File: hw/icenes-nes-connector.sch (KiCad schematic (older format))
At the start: 5 parts

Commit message: .
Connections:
- net FPGA_CPU_D7: no longer U?.26 (2A8)
- net NES_CPU_D7: no longer U?.23 (2B8)
- net NES_PPU_D7: now also U?.23 (2B8)
- new net FPGA_PPU_D7: U?.26 (2A8)
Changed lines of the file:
@@
 FPGA_PPU_D6
 Text GLabel 1550 5800 0    50   BiDi ~ 0
-FPGA_CPU_D7
+FPGA_PPU_D7
 Text GLabel 1550 5950 0    50   Input ~ 0
 ~PPU_DATA_OE
@@
 	2850 5700 3450 5700
 Text Label 3450 5800 2    50   ~ 0
-NES_CPU_D7
+NES_PPU_D7
 Wire Wire Line
 	2850 5800 3450 5800

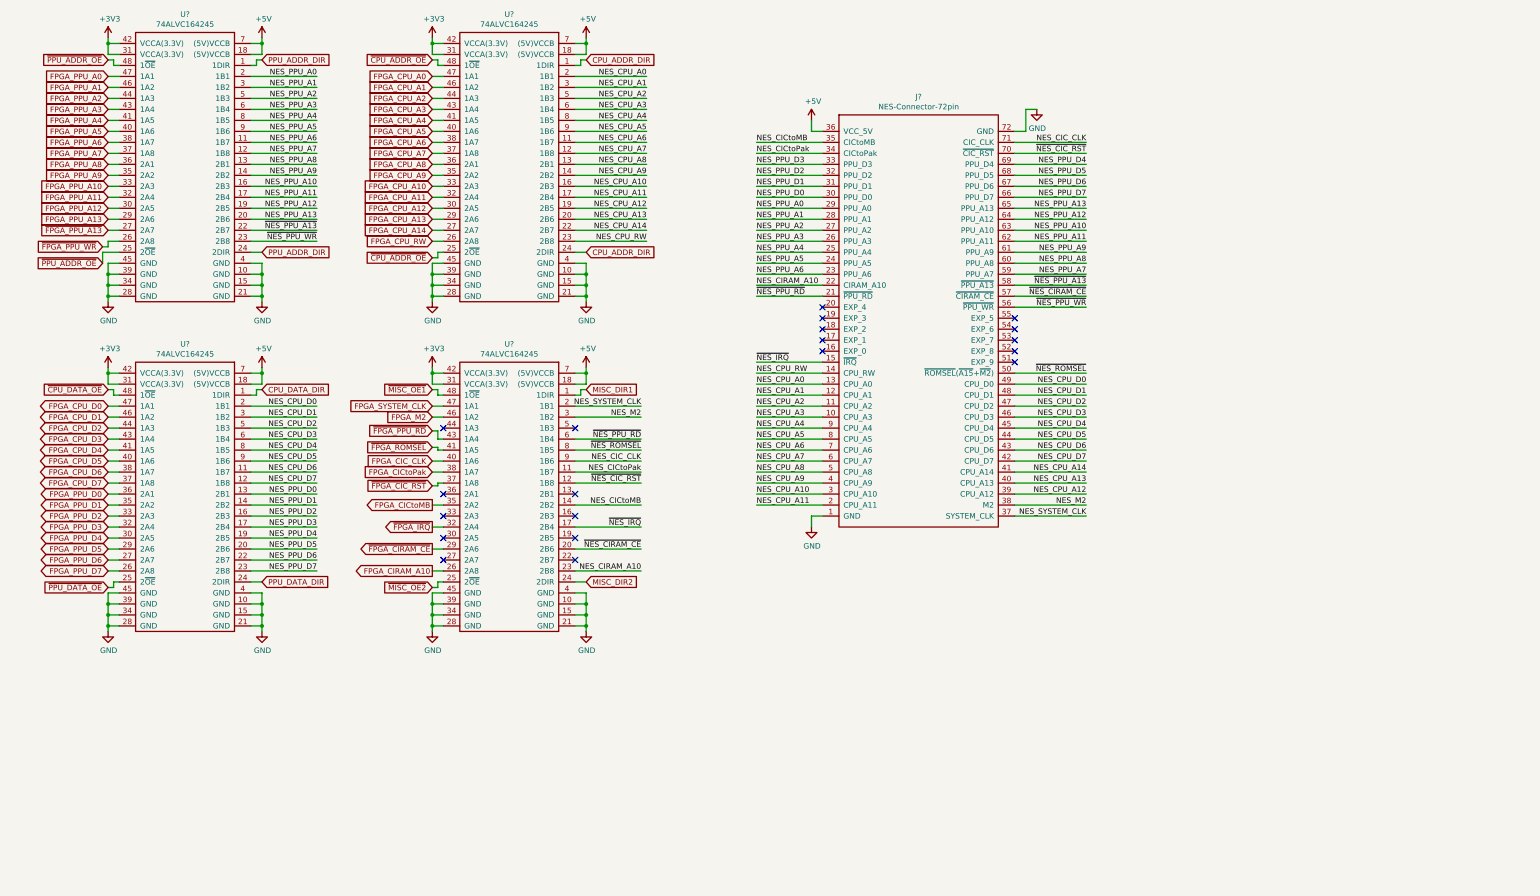
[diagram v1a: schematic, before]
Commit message: Added voltage generators for 3.3V, 1.2V and 5V. Added more info and footprints to some components. Connected signals to the NES connector to banks 0 and 1.
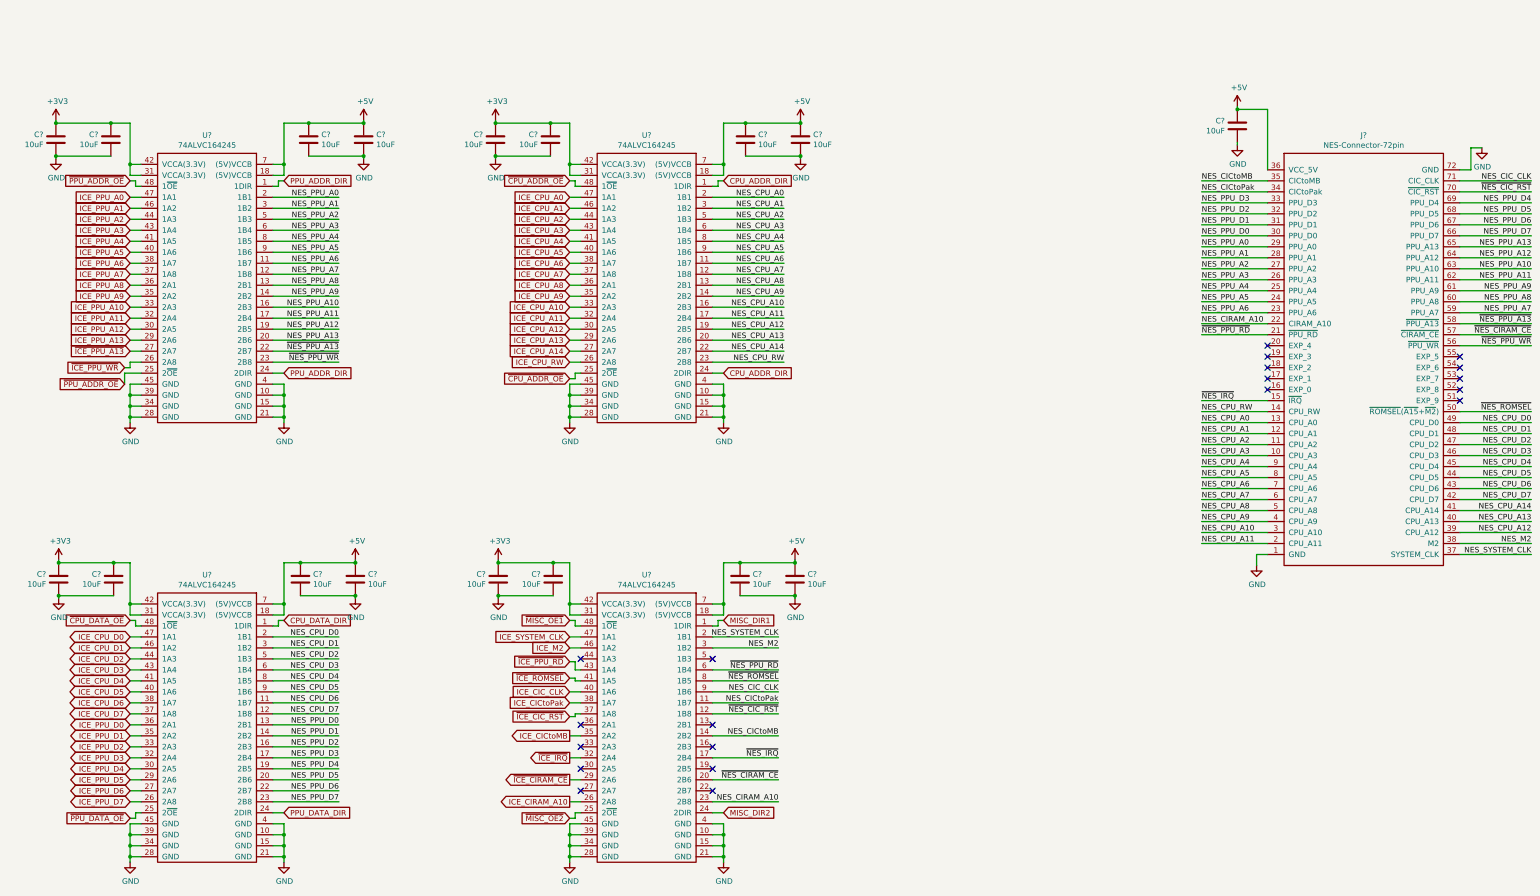
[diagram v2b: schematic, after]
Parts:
- added C? (x17): C10uF, Capacitor_SMD:C_0603_1608Metric_Pad1.05x0.95mm_HandSolder, symbol icenes-library:C10uF
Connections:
- net +3V3: now also C?.2, C?.2, C?.2, C?.2, C?.2, C?.2, C?.2, C?.2
- net +5V: now also C?.1, C?.1, C?.1, C?.1, C?.1, C?.1, C?.1, C?.1, C?.2
- net GND: now also C?.1, C?.1, C?.1, C?.1, C?.1, C?.1, C?.1, C?.1, C?.1, C?.2, C?.2, C?.2, C?.2, C?.2, C?.2, C?.2, C?.2
- net FPGA_CIC_CLK renamed ICE_CIC_CLK
- net FPGA_CICtoMB renamed ICE_CICtoMB
- net FPGA_CICtoPak renamed ICE_CICtoPak
- net FPGA_CIRAM_A10 renamed ICE_CIRAM_A10
- net FPGA_CPU_A0 renamed ICE_CPU_A0
- net FPGA_CPU_A1 renamed ICE_CPU_A1
- net FPGA_CPU_A10 renamed ICE_CPU_A10
- net FPGA_CPU_A11 renamed ICE_CPU_A11
- net FPGA_CPU_A12 renamed ICE_CPU_A12
- net FPGA_CPU_A13 renamed ICE_CPU_A13
- net FPGA_CPU_A14 renamed ICE_CPU_A14
- net FPGA_CPU_A2 renamed ICE_CPU_A2
- net FPGA_CPU_A3 renamed ICE_CPU_A3
- net FPGA_CPU_A4 renamed ICE_CPU_A4
- net FPGA_CPU_A5 renamed ICE_CPU_A5
- net FPGA_CPU_A6 renamed ICE_CPU_A6
- net FPGA_CPU_A7 renamed ICE_CPU_A7
- net FPGA_CPU_A8 renamed ICE_CPU_A8
- net FPGA_CPU_A9 renamed ICE_CPU_A9
- net FPGA_CPU_D0 renamed ICE_CPU_D0
- net FPGA_CPU_D1 renamed ICE_CPU_D1
- net FPGA_CPU_D2 renamed ICE_CPU_D2
- net FPGA_CPU_D3 renamed ICE_CPU_D3
- net FPGA_CPU_D4 renamed ICE_CPU_D4
- net FPGA_CPU_D5 renamed ICE_CPU_D5
- net FPGA_CPU_D6 renamed ICE_CPU_D6
- net FPGA_CPU_D7 renamed ICE_CPU_D7
- net FPGA_CPU_RW renamed ICE_CPU_RW
- net FPGA_M2 renamed ICE_M2
- net FPGA_PPU_A0 renamed ICE_PPU_A0
- net FPGA_PPU_A1 renamed ICE_PPU_A1
- net FPGA_PPU_A10 renamed ICE_PPU_A10
- net FPGA_PPU_A11 renamed ICE_PPU_A11
- net FPGA_PPU_A12 renamed ICE_PPU_A12
- net FPGA_PPU_A13 renamed ICE_PPU_A13
- net FPGA_PPU_A2 renamed ICE_PPU_A2
- net FPGA_PPU_A3 renamed ICE_PPU_A3
- net FPGA_PPU_A4 renamed ICE_PPU_A4
- net FPGA_PPU_A5 renamed ICE_PPU_A5
- net FPGA_PPU_A6 renamed ICE_PPU_A6
- net FPGA_PPU_A7 renamed ICE_PPU_A7
- net FPGA_PPU_A8 renamed ICE_PPU_A8
- net FPGA_PPU_A9 renamed ICE_PPU_A9
- net FPGA_PPU_D0 renamed ICE_PPU_D0
- net FPGA_PPU_D1 renamed ICE_PPU_D1
- net FPGA_PPU_D2 renamed ICE_PPU_D2
- net FPGA_PPU_D3 renamed ICE_PPU_D3
- net FPGA_PPU_D4 renamed ICE_PPU_D4
- net FPGA_PPU_D5 renamed ICE_PPU_D5
- net FPGA_PPU_D6 renamed ICE_PPU_D6
- net FPGA_PPU_D7 renamed ICE_PPU_D7
- net FPGA_SYSTEM_CLK renamed ICE_SYSTEM_CLK
- net ~FPGA_CIC_RST renamed ~ICE_CIC_RST
- net ~FPGA_CIRAM_CE renamed ~ICE_CIRAM_CE
- net ~FPGA_IRQ renamed ~ICE_IRQ
- net ~FPGA_PPU_A13 renamed ~ICE_PPU_A13
- net ~FPGA_PPU_RD renamed ~ICE_PPU_RD
- net ~FPGA_PPU_WR renamed ~ICE_PPU_WR
- net ~FPGA_ROMSEL renamed ~ICE_ROMSEL
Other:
- moved on the sheet: J?, U?

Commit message: Footprints.
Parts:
- U? (x4): footprint (none) -> Package_SO:TSSOP-48_6.1x12.5mm_P0.5mm; Manufacturer (none) -> IDT; Part number (none) -> 74ALVC164245PAG8
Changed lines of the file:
@@
 F 0 "U?" H 2450 2065 50  0000 C CNN
 F 1 "74ALVC164245" H 2450 1974 50  0000 C CNN
-F 2 "" H 2450 1950 50  0001 C CNN
+F 2 "Package_SO:TSSOP-48_6.1x12.5mm_P0.5mm" H 2450 1950 50  0001 C CNN
 F 3 "https://www.idt.com/document/dst/74alvc164245-datasheet" H 2450 1950 50  0001 C CNN
+F 4 "IDT " H 2450 1950 50  0001 C CNN "Manufacturer"
+F 5 "74ALVC164245PAG8" H 2450 1950 50  0001 C CNN "Part number"
 	1    2450 1950
 	-1   0    0    -1
@@
 F 0 "U?" H 2450 6065 50  0000 C CNN
 F 1 "74ALVC164245" H 2450 5974 50  0000 C CNN
-F 2 "" H 2450 5950 50  0001 C CNN
+F 2 "Package_SO:TSSOP-48_6.1x12.5mm_P0.5mm" H 2450 5950 50  0001 C CNN
 F 3 "https://www.idt.com/document/dst/74alvc164245-datasheet" H 2450 5950 50  0001 C CNN
+F 4 "IDT " H 2450 5950 50  0001 C CNN "Manufacturer"
+F 5 "74ALVC164245PAG8" H 2450 5950 50  0001 C CNN "Part number"
 	1    2450 5950
 	-1   0    0    -1
@@
 F 0 "U?" H 6450 6065 50  0000 C CNN
 F 1 "74ALVC164245" H 6450 5974 50  0000 C CNN
-F 2 "" H 6450 5950 50  0001 C CNN
+F 2 "Package_SO:TSSOP-48_6.1x12.5mm_P0.5mm" H 6450 5950 50  0001 C CNN
 F 3 "https://www.idt.com/document/dst/74alvc164245-datasheet" H 6450 5950 50  0001 C CNN
+F 4 "IDT " H 6450 5950 50  0001 C CNN "Manufacturer"
+F 5 "74ALVC164245PAG8" H 6450 5950 50  0001 C CNN "Part number"
 	1    6450 5950
 	-1   0    0    -1
@@
 F 0 "U?" H 6450 2065 50  0000 C CNN
 F 1 "74ALVC164245" H 6450 1974 50  0000 C CNN
-F 2 "" H 6450 1950 50  0001 C CNN
+F 2 "Package_SO:TSSOP-48_6.1x12.5mm_P0.5mm" H 6450 1950 50  0001 C CNN
 F 3 "https://www.idt.com/document/dst/74alvc164245-datasheet" H 6450 1950 50  0001 C CNN
+F 4 "IDT " H 6450 1950 50  0001 C CNN "Manufacturer"
+F 5 "74ALVC164245PAG8" H 6450 1950 50  0001 C CNN "Part number"
 	1    6450 1950
 	-1   0    0    -1

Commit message: Footprints.
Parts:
- J?: footprint (none) -> icenes-library:DIP-72-NES-CONNECTOR
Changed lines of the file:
@@
 F 0 "J?" H 12975 2065 50  0000 C CNN
 F 1 "NES-Connector-72pin" H 12975 1974 50  0000 C CNN
-F 2 "" H 12950 1950 50  0001 C CNN
+F 2 "icenes-library:DIP-72-NES-CONNECTOR" H 12950 1950 50  0001 C CNN
 F 3 "" H 12950 1950 50  0001 C CNN
 	1    12950 1950

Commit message: Minor fixes.
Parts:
- gave numbers to parts that had none: 22
